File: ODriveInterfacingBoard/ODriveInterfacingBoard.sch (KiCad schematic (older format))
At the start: 48 parts, among them U1 ODrive, U2 MAX3077E

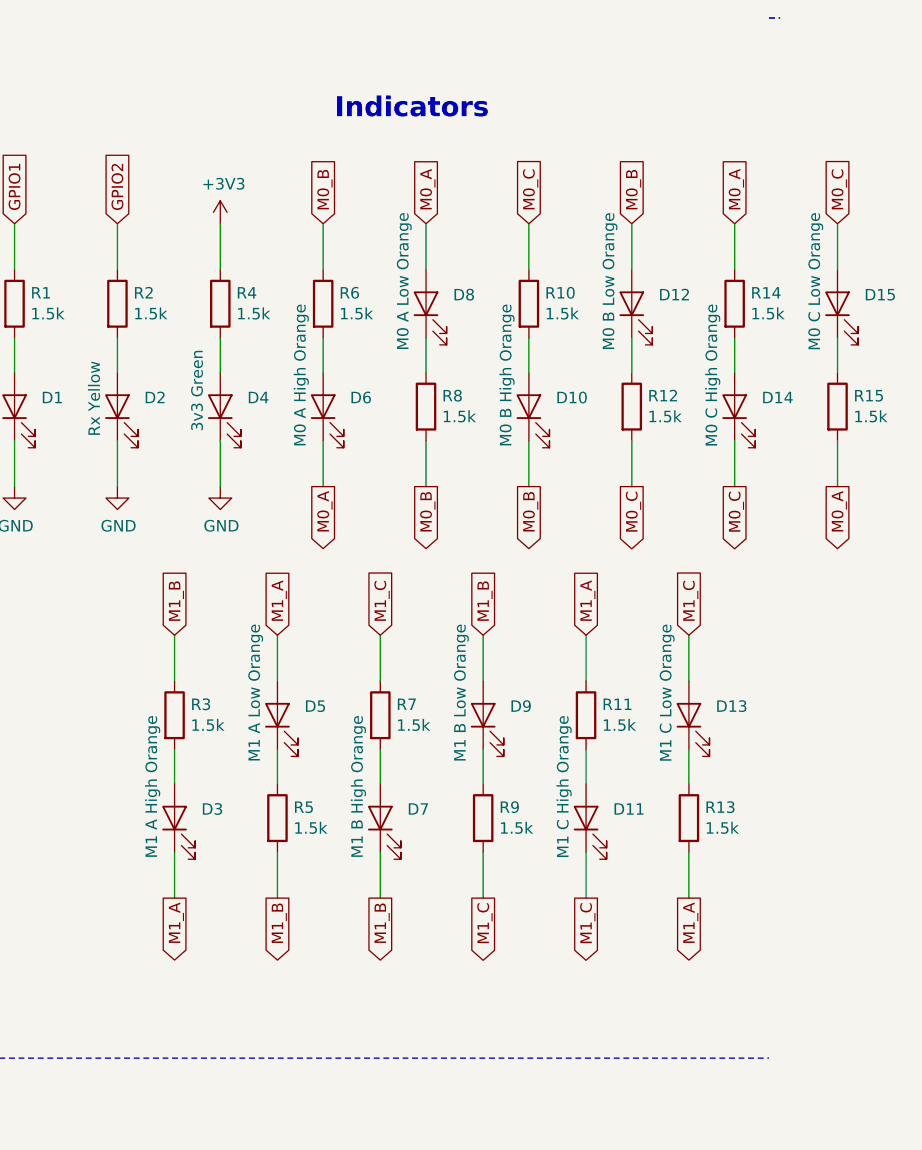
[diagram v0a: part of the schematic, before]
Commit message: Fixed LED traces
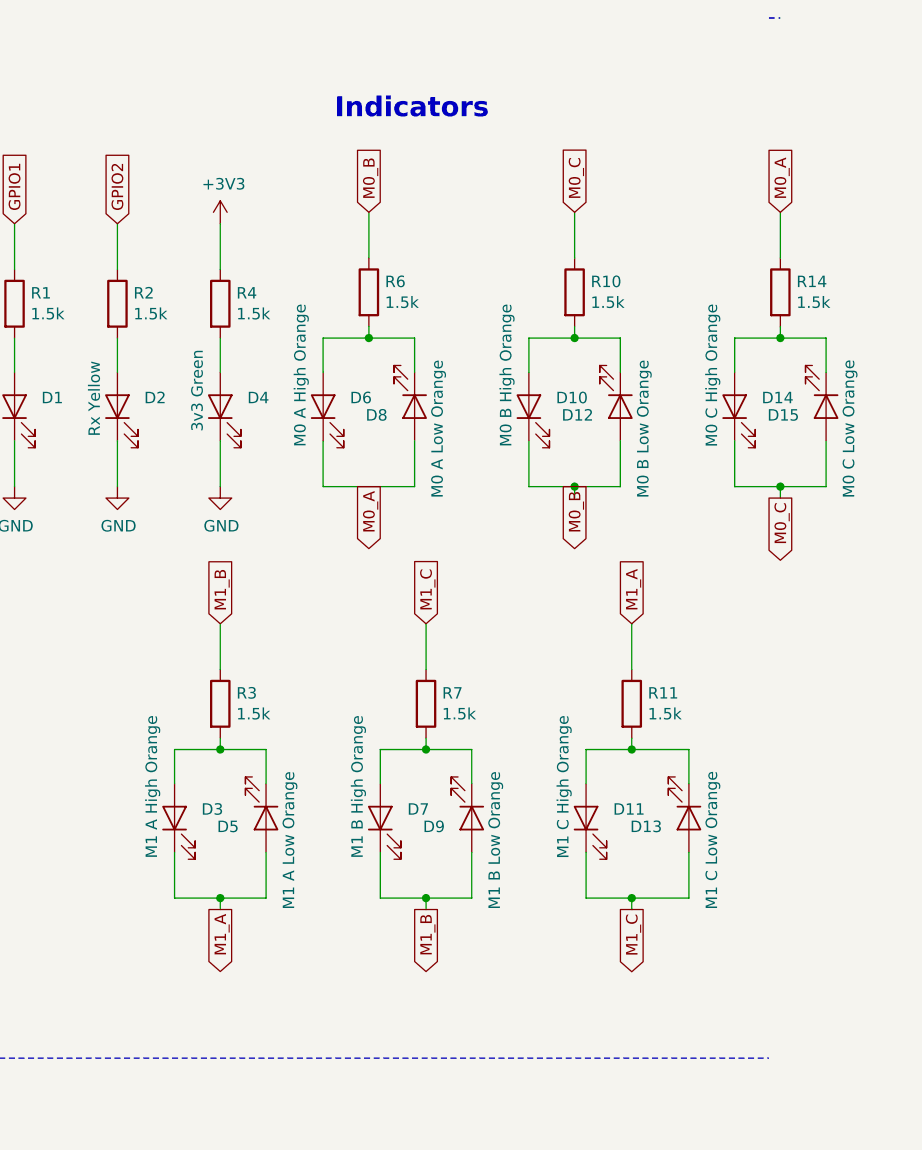
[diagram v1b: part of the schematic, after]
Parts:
- removed R12, R13, R15, R5, R8, R9: 1.5k, Resistor_SMD:R_0603_1608Metric_Pad1.05x0.95mm_HandSolder, symbol Device:R
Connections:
- net at D3.2 (A), R3.2: now also D5.1 (K)
- net at D7.2 (A), R7.2: now also D9.1 (K)
- net at D11.2 (A), R11.2: now also D13.1 (K)
- net at D6.2 (A), R6.2: now also D8.1 (K)
- net at D10.2 (A), R10.2: now also D12.1 (K)
- net at D14.2 (A), R14.2: now also D15.1 (K)
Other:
- moved on the sheet: D12, D13, D15, D5, D8, D9, R10, R11, R14, R3, R6, R7

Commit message: Added silkscreen
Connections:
- net GPIO1 is gone; now on net Tx: R1.1
- net GPIO2 is gone; now on net Rx: R2.1
- net E1_GND: now also Conn5.2
- net Rx: no longer Conn9.3, R17.1
- net Tx: no longer Conn9.1, R16.1
- net AGND: now reaches Conn1.1, U1.AGND
- net AVCC: now reaches Conn1.2, U1.AVCC
- net Y: now reaches Conn10.5, U2.5 (Y)
- net Z: now reaches Conn10.4, U2.6 (Z)
- net B: now reaches Conn10.2, R18.1, U2.7 (B)
- net A: now reaches Conn10.1, R18.2, U2.8 (A)
- net E0_GND: no longer names the net of U1.E0_GND
- net E0_GND: no longer Conn5.2
- new net: Conn9.1, R16.1
- new net: Conn9.3, R17.1
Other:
- moved on the sheet: R16, R17
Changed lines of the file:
@@
 	2800 2700 2650 2700
 Wire Wire Line
-	2650 3200 2800 3200
-Wire Wire Line
-	2000 3200 2150 3200
+	2000 3200 2100 3200
 $Comp
 L MRDT_Connectors:Molex_SL_07 Conn6
@@
 L power:GND #PWR013
 U 1 1 5C74723B
-P 4300 1800
-F 0 "#PWR013" H 4300 1550 50  0001 C CNN
-F 1 "GND" V 4305 1672 50  0000 R CNN
-F 2 "" H 4300 1800 50  0001 C CNN
-F 3 "" H 4300 1800 50  0001 C CNN
-	1    4300 1800
+P 3850 1850
+F 0 "#PWR013" H 3850 1600 50  0001 C CNN
+F 1 "GND" V 3855 1722 50  0000 R CNN
+F 2 "" H 3850 1850 50  0001 C CNN
+F 3 "" H 3850 1850 50  0001 C CNN
+	1    3850 1850
 	1    0    0    -1
 $EndComp
@@
 NoConn ~ 2800 3300
 NoConn ~ 4550 2950
-Text Label 2800 1800 0    49   ~ 0
-Tx
-Text Label 2800 1900 0    49   ~ 0
-Rx
 Text Label 2650 2700 0    49   ~ 0
 E0_3V3
@@
 Text Label 2650 3100 0    49   ~ 0
 E0_Z
-Text Label 2650 3200 0    49   ~ 0
-E0_GND
 Text Label 2000 2700 0    49   ~ 0
 E1_3V3
@@
 Wire Wire Line
 	9650 3100 9650 3300
+Text GLabel 7400 1350 1    50   Input ~ 0
+Rx
 Text GLabel 6950 1350 1    50   Input ~ 0
-GPIO1
-Text GLabel 7400 1350 1    50   Input ~ 0
-GPIO2
+Tx
 Wire Wire Line
 	6950 1350 6950 1550
@@
 L Device:R R16
 U 1 1 5C7E4FB3
-P 3200 1800
-F 0 "R16" V 3100 1800 50  0000 C CNN
-F 1 "0" V 3200 1800 50  0000 C CNN
-F 2 "Resistor_SMD:R_0603_1608Metric_Pad1.05x0.95mm_HandSolder" V 3130 1800 50  0001 C CNN
-F 3 "~" H 3200 1800 50  0001 C CNN
-	1    3200 1800
+P 4350 1700
+F 0 "R16" V 4250 1700 50  0000 C CNN
+F 1 "0" V 4350 1700 50  0000 C CNN
+F 2 "Resistor_SMD:R_0603_1608Metric_Pad1.05x0.95mm_HandSolder" V 4280 1700 50  0001 C CNN
+F 3 "~" H 4350 1700 50  0001 C CNN
+	1    4350 1700
 	0    1    1    0
 $EndComp
@@
 L Device:R R17
 U 1 1 5C7E5124
-P 3200 1900
-F 0 "R17" V 3300 1900 50  0000 C CNN
-F 1 "0" V 3200 1900 50  0000 C CNN
-F 2 "Resistor_SMD:R_0603_1608Metric_Pad1.05x0.95mm_HandSolder" V 3130 1900 50  0001 C CNN
-F 3 "~" H 3200 1900 50  0001 C CNN
-	1    3200 1900
+P 4350 1900
+F 0 "R17" V 4450 1900 50  0000 C CNN
+F 1 "0" V 4350 1900 50  0000 C CNN
+F 2 "Resistor_SMD:R_0603_1608Metric_Pad1.05x0.95mm_HandSolder" V 4280 1900 50  0001 C CNN
+F 3 "~" H 4350 1900 50  0001 C CNN
+	1    4350 1900
 	0    1    1    0
 $EndComp
@@
 Wire Wire Line
 	3900 850  3900 800
-Text GLabel 3450 1800 2    50   Output ~ 0
+Text GLabel 3050 1800 2    50   Output ~ 0
 Tx
-Text GLabel 3450 1900 2    50   Input ~ 0
+Text GLabel 3050 1900 2    50   Input ~ 0
 Rx
 Text GLabel 3900 950  0    50   Input ~ 0
@@
 Wire Wire Line
 	2650 1900 3050 1900
-Wire Wire Line
-	3350 1900 3450 1900
-Wire Wire Line
-	3350 1800 3450 1800
 Text GLabel 2100 2300 0    50   Output ~ 0
 CAN_H
@@
 Wire Wire Line
 	3950 1050 3900 1050
-Text GLabel 4500 1700 0    50   Input ~ 0
+Text GLabel 4150 1700 0    50   Input ~ 0
 Tx
-Text GLabel 4500 1900 0    50   Output ~ 0
+Text GLabel 4150 1900 0    50   Output ~ 0
 Rx
 Wire Wire Line
@@
 	1    0    0    -1
 $EndComp
-Wire Wire Line
-	4300 1800 4550 1800
 $Comp
 L ODriveInterfacingBoard-rescue:power_GND-ODriveInterfacingBoard-cache #PWR0101
@@
 Wire Wire Line
 	9650 4300 9450 4300
+Wire Wire Line
+	2800 3200 2700 3200
+Wire Wire Line
+	2700 3200 2700 3350
+Wire Wire Line
+	2700 3350 2100 3350
+Wire Wire Line
+	2100 3350 2100 3200
+Connection ~ 2100 3200
+Wire Wire Line
+	2100 3200 2150 3200
+Wire Wire Line
+	4200 1700 4150 1700
+Wire Wire Line
+	4150 1900 4200 1900
+Wire Wire Line
+	3850 1800 3850 1850
+Wire Wire Line
+	3850 1800 4550 1800
+Text Label 4950 850  0    50   ~ 0
+A
+Text Label 4950 950  0    50   ~ 0
+B
+Text Label 4950 1150 0    50   ~ 0
+Z
+Text Label 4950 1250 0    50   ~ 0
+Y
+Text Label 2000 1700 0    50   ~ 0
+AVCC
+Text Label 2000 1800 0    50   ~ 0
+AGND
 $EndSCHEMATC

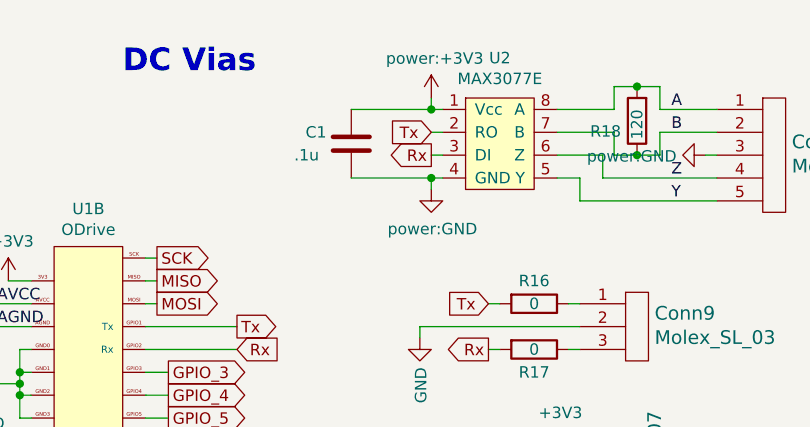
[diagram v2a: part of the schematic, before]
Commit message: Fixed Tx Rx issue
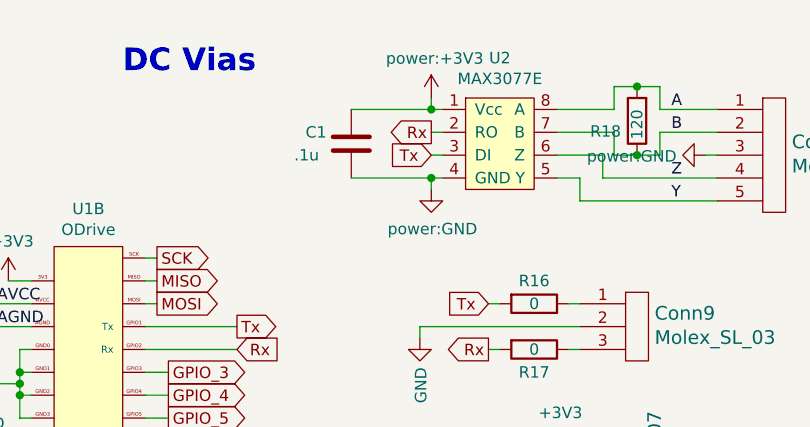
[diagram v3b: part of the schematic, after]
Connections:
- net Rx: now also U2.2 (RO); no longer U2.3 (DI)
- net Tx: now also U2.3 (DI); no longer U2.2 (RO)
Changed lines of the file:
@@
 Text GLabel 3050 1900 2    50   Input ~ 0
 Rx
-Text GLabel 3900 950  0    50   Input ~ 0
+Text GLabel 3900 1050 0    50   Input ~ 0
 Tx
-Text GLabel 3900 1050 0    50   Output ~ 0
+Text GLabel 3900 950  0    50   Output ~ 0
 Rx
 Wire Wire Line
